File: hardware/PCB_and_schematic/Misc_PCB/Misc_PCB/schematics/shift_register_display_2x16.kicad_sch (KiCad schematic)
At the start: 15 parts, among them J4 LCD_CONN, J6 LCD_DISPLAY, Q8 BC547, U4 74HC595

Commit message: progress with esp power pcb
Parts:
- removed J6: LCD_DISPLAY, Connector_PinHeader_2.54mm:PinHeader_2x09_P2.54mm_Vertical, symbol Connector_Generic:Conn_02x09_Odd_Even
- added J18: LCD16x2, symbol Connector_Generic:Conn_01x16
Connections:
- net +5V: now also J18.1 (Pin_1), J18.15 (Pin_15)
- net GND: now also J18.2 (Pin_2), J18.5 (Pin_5)
- net at R13.1, R17.1, R8.1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: now also J18.16 (Pin_16)
- net at RV1.2: now also J18.3 (Pin_3)
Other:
- note added: "GND VDD VEE RS RW EN D0 D1 D2 D3 D4 D5 D6 D7 LED+ LED-"
- moved on the sheet: Q8, R11, R13, R14, R15, R17, R8, R9, RV1

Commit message: Shift register for LCD update
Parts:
- added R70, R75, R76, R77: 10k, Resistor_SMD:R_0805_2012Metric, symbol Device:R
- J19: renamed from J18; footprint (none) -> Connector_PinSocket_2.54mm:PinSocket_1x16_P2.54mm_Vertical
- Q8: footprint Package_TO_SOT_THT:TO-92_Inline -> My-Footprints:TO-92_Inline_LITTLE_BIGGER
- renumbered C2 to C19, J4 to J18, R11 to R67, R8 to R80, R9 to R81
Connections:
- net DB4 is gone; now on net DB4_A: U4.4 (QE)
- net DB5 is gone; now on net DB5_A: U4.3 (QD)
- net DB6 is gone; now on net DB6_A: U4.2 (QC)
- net DB7 is gone; now on net DB7_A: U4.1 (QB)
- net E2 is gone; now on net EN: U4.5 (QF)
- net RS is gone; now on net RS_A: U4.6 (QG)
- net GND: now also R70.1, R75.1, R76.1, R77.1
- net at J19.10 (Pin_10): now also R77.2
- net DB4_A: now reaches J19.11 (Pin_11)
- net DB5_A: now reaches J19.12 (Pin_12)
- net DB6_A: now reaches J19.13 (Pin_13)
- net DB7_A: now reaches J19.14 (Pin_14)
- net RS_A: now reaches J19.4 (Pin_4)
- net EN: now reaches J19.6 (Pin_6)
- net at J19.7 (Pin_7): now also R70.2
- net at J19.8 (Pin_8): now also R75.2
- net at J19.9 (Pin_9): now also R76.2
- net BACKLIGHT_DRIVE renamed BACKLIGHT_DRIVE_A
- net E1: no longer names the net of U4.7 (QH)
- no-connect marks 1 -> 0
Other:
- note added: "4x10k"
- moved on the sheet: J19, Q8, R13, R14, R15, R17, R67, R80, R81, RV1

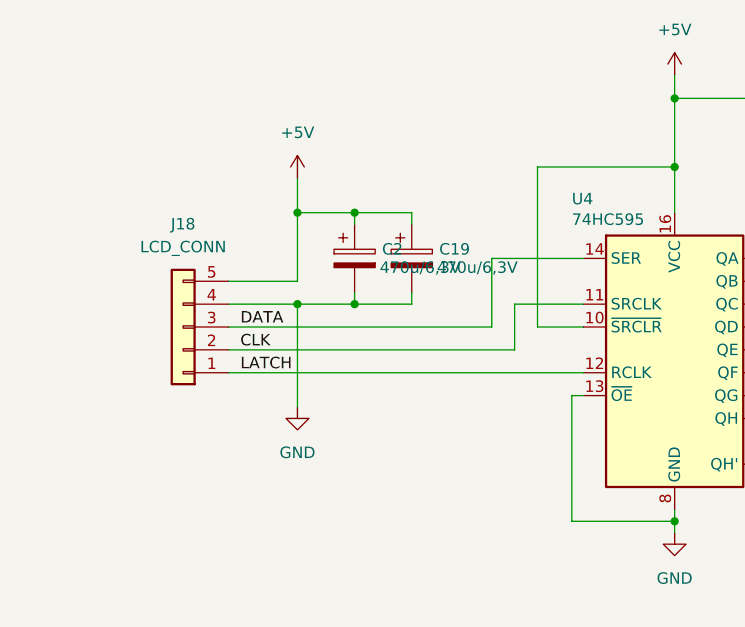
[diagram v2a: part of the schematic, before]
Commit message: add footprint association
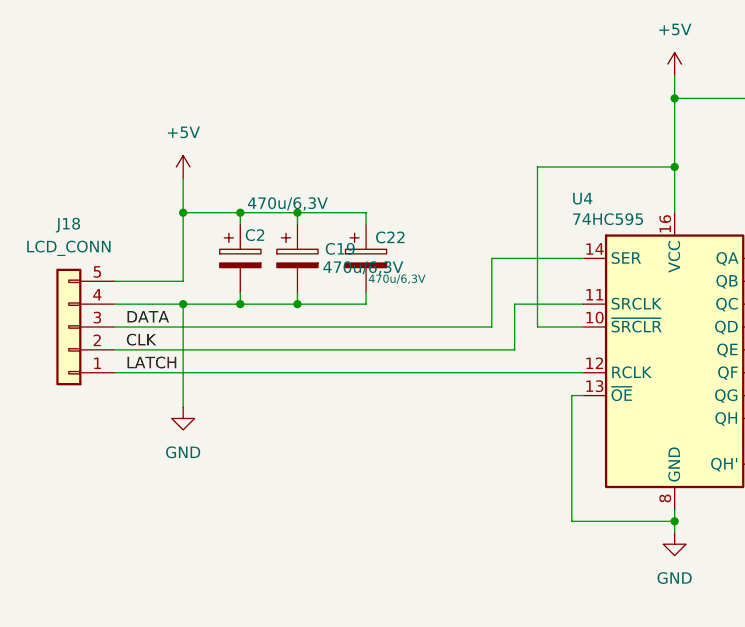
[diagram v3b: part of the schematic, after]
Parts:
- added C22: 470u/6,3V, Capacitor_SMD:CP_Elec_5x5.7, symbol Device:C_Polarized
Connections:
- net +5V: now also C22.1
- net GND: now also C22.2
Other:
- moved on the sheet: C19, C2, J18

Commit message: update power tracking heater
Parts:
- renumbered C19 to C20, C22 to C21, J18 to J19, J19 to J20, R67 to R71, R70 to R74
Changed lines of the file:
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@@
 			(project "Misc_PCB"
 				(path "/7b59bc46-701c-4caa-9db8-f0eec290561d/6436e512-c247-470c-9775-a9b90aba82b0"
-					(reference "#PWR0110")
+					(reference "#PWR0114")
 					(unit 1)
 				)
@@
 		(dnp no)
 		(fields_autoplaced yes)
-		(property "Reference" "#PWR0100"
+		(property "Reference" "#PWR0112"
 			(at 203.2 83.82 0)
 			(effects
@@
 			(project "Misc_PCB"
 				(path "/7b59bc46-701c-4caa-9db8-f0eec290561d/6436e512-c247-470c-9775-a9b90aba82b0"
-					(reference "#PWR0100")
+					(reference "#PWR0112")
 					(unit 1)
 				)
@@
 		(on_board yes)
 		(dnp no)
-		(property "Reference" "J19"
+		(property "Reference" "J20"
 			(at 212.09 28.448 0)
 			(effects
@@
 			(project "Misc_PCB"
 				(path "/7b59bc46-701c-4caa-9db8-f0eec290561d/6436e512-c247-470c-9775-a9b90aba82b0"
-					(reference "J19")
+					(reference "J20")
 					(unit 1)
 				)
@@
 		(on_board yes)
 		(dnp no)
-		(property "Reference" "C19"
+		(property "Reference" "C20"
 			(at 44.958 43.434 0)
 			(effects
@@
 			(project "Misc_PCB"
 				(path "/7b59bc46-701c-4caa-9db8-f0eec290561d/6436e512-c247-470c-9775-a9b90aba82b0"
-					(reference "C19")
+					(reference "C20")
 					(unit 1)
 				)
@@
 		(on_board yes)
 		(dnp no)
-		(property "Reference" "C22"
+		(property "Reference" "C21"
 			(at 50.546 42.164 0)
 			(effects
@@
 			(project "Misc_PCB"
 				(path "/7b59bc46-701c-4caa-9db8-f0eec290561d/6436e512-c247-470c-9775-a9b90aba82b0"
-					(reference "C22")
+					(reference "C21")
 					(unit 1)
 				)
@@
 			(project "Misc_PCB"
 				(path "/7b59bc46-701c-4caa-9db8-f0eec290561d/6436e512-c247-470c-9775-a9b90aba82b0"
-					(reference "#PWR0106")
+					(reference "#PWR0110")
 					(unit 1)
 				)
@@
 			(project "Misc_PCB"
 				(path "/7b59bc46-701c-4caa-9db8-f0eec290561d/6436e512-c247-470c-9775-a9b90aba82b0"
-					(reference "U13")
+					(reference "U14")
 					(unit 1)
 				)
@@
 			(project "Misc_PCB"
 				(path "/7b59bc46-701c-4caa-9db8-f0eec290561d/6436e512-c247-470c-9775-a9b90aba82b0"
-					(reference "RV2")
+					(reference "RV3")
 					(unit 1)
 				)
@@
 			(project "Misc_PCB"
 				(path "/7b59bc46-701c-4caa-9db8-f0eec290561d/6436e512-c247-470c-9775-a9b90aba82b0"
-					(reference "#PWR0104")
+					(reference "#PWR0113")
 					(unit 1)
 				)
@@
 			(project "Misc_PCB"
 				(path "/7b59bc46-701c-4caa-9db8-f0eec290561d/6436e512-c247-470c-9775-a9b90aba82b0"
-					(reference "#PWR0108")
+					(reference "#PWR0107")
 					(unit 1)
 				)
@@
 			(project "Misc_PCB"
 				(path "/7b59bc46-701c-4caa-9db8-f0eec290561d/6436e512-c247-470c-9775-a9b90aba82b0"
-					(reference "R69")
+					(reference "R73")
 					(unit 1)
 				)
@@
 			(project "Misc_PCB"
 				(path "/7b59bc46-701c-4caa-9db8-f0eec290561d/6436e512-c247-470c-9775-a9b90aba82b0"
-					(reference "#PWR0105")
+					(reference "#PWR0111")
 					(unit 1)
 				)
@@
 			(project "Misc_PCB"
 				(path "/7b59bc46-701c-4caa-9db8-f0eec290561d/6436e512-c247-470c-9775-a9b90aba82b0"
-					(reference "#PWR0102")
+					(reference "#PWR0105")
 					(unit 1)
 				)
@@
 		(dnp no)
 		(fields_autoplaced yes)
-		(property "Reference" "J18"
+		(property "Reference" "J19"
 			(at 16.51 40.64 0)
 			(effects
@@
 			(project "Misc_PCB"
 				(path "/7b59bc46-701c-4caa-9db8-f0eec290561d/6436e512-c247-470c-9775-a9b90aba82b0"
-					(reference "J18")
+					(reference "J19")
 					(unit 1)
 				)
@@
 			(project "Misc_PCB"
 				(path "/7b59bc46-701c-4caa-9db8-f0eec290561d/6436e512-c247-470c-9775-a9b90aba82b0"
-					(reference "C20")
+					(reference "C22")
 					(unit 1)
 				)
@@
 			(project "Misc_PCB"
 				(path "/7b59bc46-701c-4caa-9db8-f0eec290561d/6436e512-c247-470c-9775-a9b90aba82b0"
-					(reference "#PWR0109")
+					(reference "#PWR0108")
 					(unit 1)
 				)
@@
 			(project "Misc_PCB"
 				(path "/7b59bc46-701c-4caa-9db8-f0eec290561d/6436e512-c247-470c-9775-a9b90aba82b0"
-					(reference "#PWR0107")
+					(reference "#PWR0109")
 					(unit 1)
 				)
@@
 			(project "Misc_PCB"
 				(path "/7b59bc46-701c-4caa-9db8-f0eec290561d/6436e512-c247-470c-9775-a9b90aba82b0"
-					(reference "R68")
+					(reference "R72")
 					(unit 1)
 				)
@@
 		(on_board yes)
 		(dnp no)
-		(property "Reference" "R70"
+		(property "Reference" "R74"
 			(at 195.58 49.53 90)
 			(effects
@@
 			(project "Misc_PCB"
 				(path "/7b59bc46-701c-4caa-9db8-f0eec290561d/6436e512-c247-470c-9775-a9b90aba82b0"
-					(reference "R70")
+					(reference "R74")
 					(unit 1)
 				)
@@
 			(project "Misc_PCB"
 				(path "/7b59bc46-701c-4caa-9db8-f0eec290561d/6436e512-c247-470c-9775-a9b90aba82b0"
-					(reference "C18")
+					(reference "C19")
 					(unit 1)
 				)
@@
 			(project "Misc_PCB"
 				(path "/7b59bc46-701c-4caa-9db8-f0eec290561d/6436e512-c247-470c-9775-a9b90aba82b0"
-					(reference "#PWR0103")
+					(reference "#PWR0106")
 					(unit 1)
 				)
@@
 		(dnp no)
 		(fields_autoplaced yes)
-		(property "Reference" "R67"
+		(property "Reference" "R71"
 			(at 160.02 38.0999 0)
 			(effects
@@
 			(project "Misc_PCB"
 				(path "/7b59bc46-701c-4caa-9db8-f0eec290561d/6436e512-c247-470c-9775-a9b90aba82b0"
-					(reference "R67")
-					(unit 1)
-				)
+					(reference "R71")
+					(unit 1)
+				)
